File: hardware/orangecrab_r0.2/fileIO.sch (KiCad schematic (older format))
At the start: 29 parts, among them J1 Conn_01x12_Male, J2 Conn_01x16_Male, J3 USB_B_Micro, SW1 SW_Push, U9 CD74HC4067M

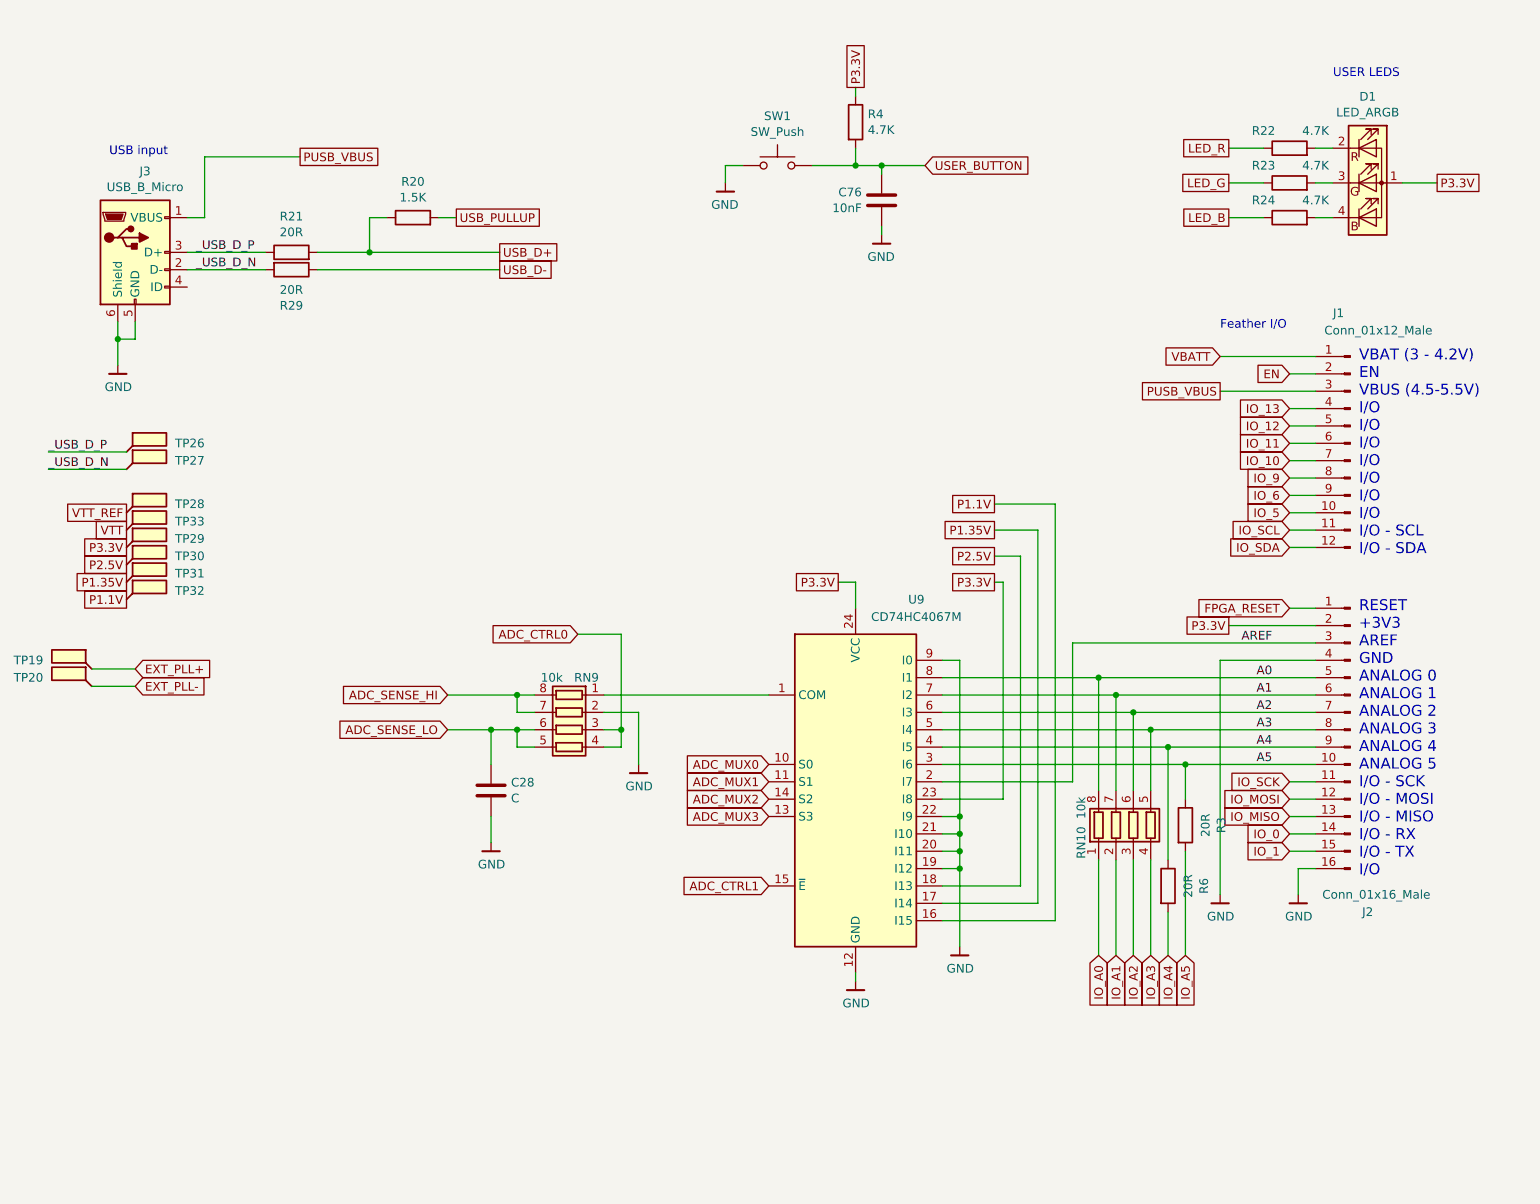
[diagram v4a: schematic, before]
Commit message: hw: Update fiducials Add pullup to FLASH CS/SCK line Update BOM part numbers Fix Button pull-up voltage
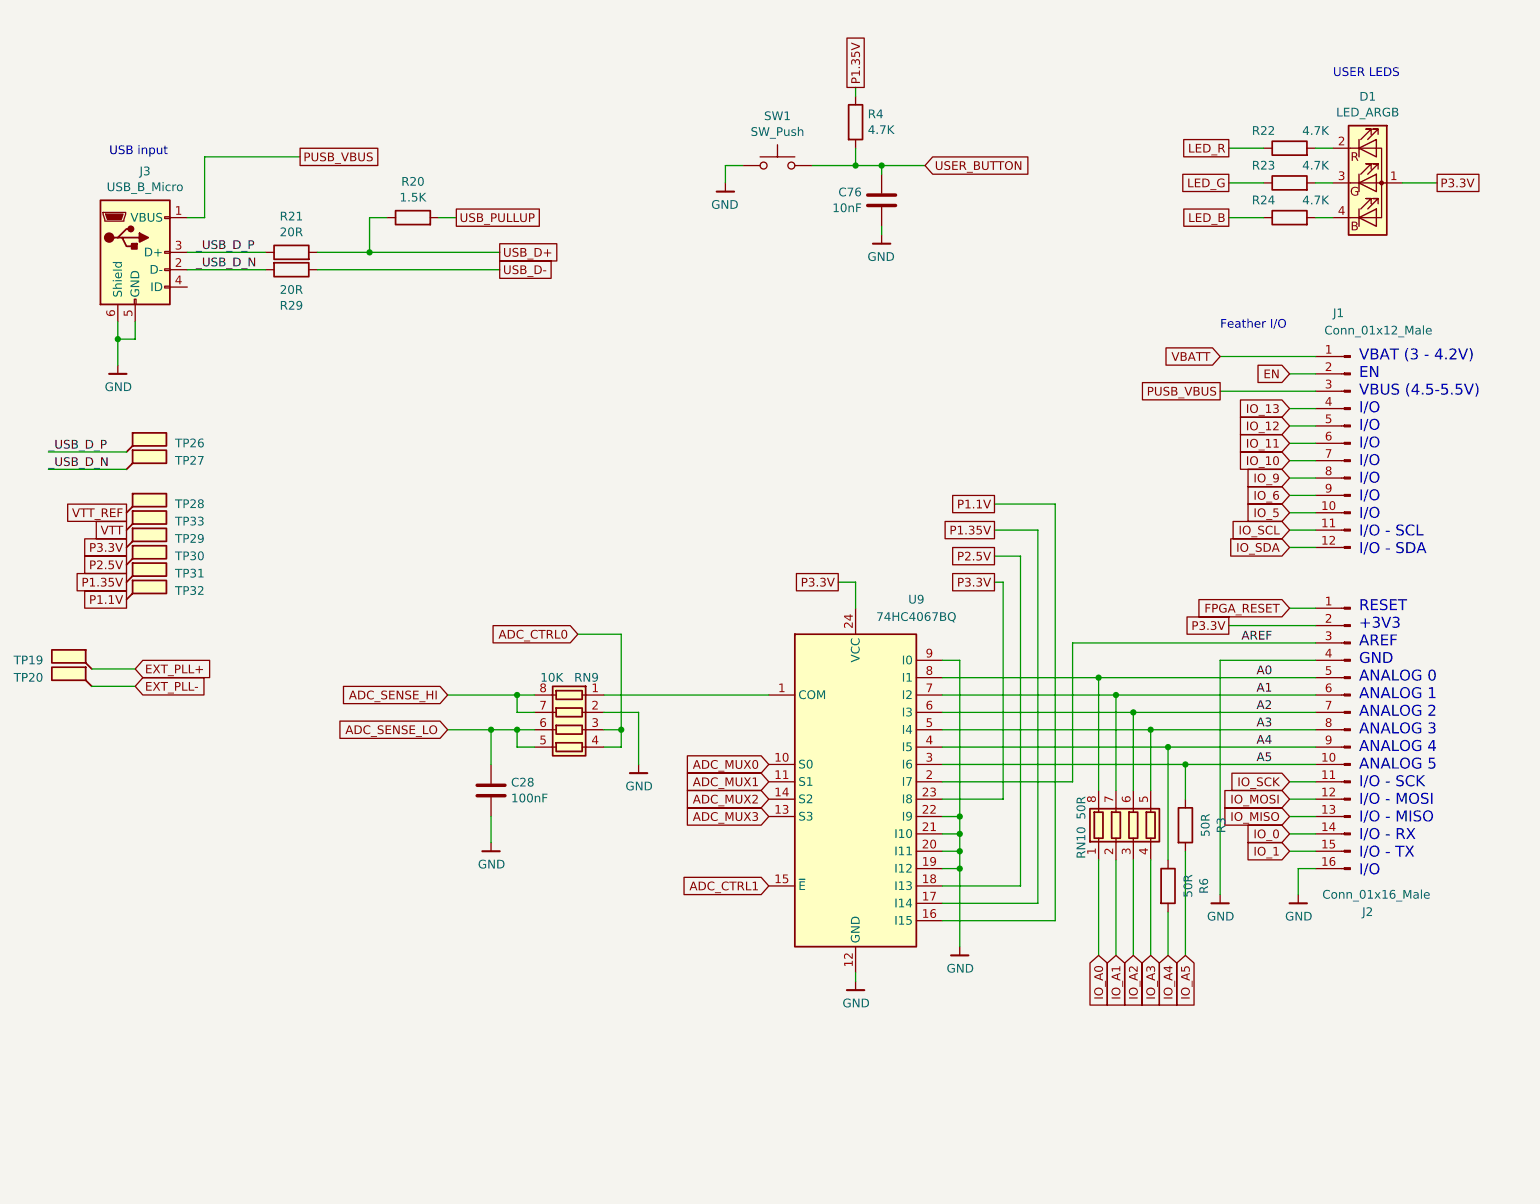
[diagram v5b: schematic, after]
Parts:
- C28: value C -> 100nF; Mfg (none) -> Samsung Electro-Mechanics; PN (none) -> CL03A104KQ3NNNC
- R21, R29: PN (none) -> RC0402FR-0720RL
- R3, R6: value 20R -> 50R; PN (none) -> RC0402FR-0750RL
- RN10: value 10k -> 50R; PN (none) -> RAVF104DJT51R0
- RN9: value 10k -> 10K; PN (none) -> RAVF104DJT10K0
- U9: value CD74HC4067M -> 74HC4067BQ; Mfg (none) -> Nexperia USA Inc.; PN (none) -> 74HC4067BQ,118
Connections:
- net P1.35V: now also R4.1
- net P3.3V: no longer R4.1
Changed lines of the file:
@@
 $EndComp
 Text GLabel 5950 800  1    50   UnSpc ~ 0
-P3.3V
+P1.35V
 $Comp
 L Device:R R4
@@
 F 3 "~" H 2700 1750 50  0001 C CNN
 F 4 "‎Yageo‎" H 2700 1750 50  0001 C CNN "Mfg"
+F 5 "RC0402FR-0720RL" H 2700 1750 50  0001 C CNN "PN"
 	1    2700 1750
 	0    -1   -1   0
@@
 F 3 "~" H 2700 1850 50  0001 C CNN
 F 4 "‎Yageo‎" H 2700 1850 50  0001 C CNN "Mfg"
+F 5 "RC0402FR-0720RL" H 2700 1850 50  0001 C CNN "PN"
 	1    2700 1850
 	0    1    1    0
@@
 P 5950 4800
 F 0 "U9" H 6300 5850 50  0000 C CNN
-F 1 "CD74HC4067M" H 6300 5750 50  0000 C CNN
+F 1 "74HC4067BQ" H 6300 5750 50  0000 C CNN
 F 2 "Package_DFN_QFN:Texas_RGY_R-PVQFN-N24_EP2.05x3.1mm" H 6850 3800 50  0001 C CIN
 F 3 "http://www.ti.com/lit/ds/symlink/cd74hc4067.pdf" H 5600 5650 50  0001 C CNN
+F 4 "Nexperia USA Inc." H 5950 4800 50  0001 C CNN "Mfg"
+F 5 "74HC4067BQ,118" H 5950 4800 50  0001 C CNN "PN"
 	1    5950 4800
 	1    0    0    -1
@@
 AR Path="/5ABC9A87/5DF38AC3" Ref="RN9"  Part="1"
 F 0 "RN9" V 4000 4400 50  0000 C CNN
-F 1 "10k" V 4000 4600 50  0000 C CNN
+F 1 "10K" V 4000 4600 50  0000 C CNN
 F 2 "Resistor_SMD:R_Array_Convex_4x0402" V 4575 4500 50  0001 C CNN
 F 3 "~" H 4300 4500 50  0001 C CNN
 F 4 "Stackpole Electronics Inc" H 4300 4500 50  0001 C CNN "Mfg"
+F 5 "RAVF104DJT10K0" H 4300 4500 50  0001 C CNN "PN"
 	1    4300 4500
 	0    -1   1    0
@@
 P 3850 4850
 F 0 "C28" H 3965 4896 50  0000 L CNN
-F 1 "C" H 3965 4805 50  0000 L CNN
+F 1 "100nF" H 3965 4805 50  0000 L CNN
 F 2 "Capacitor_SMD:C_0201_0603Metric" H 3888 4700 50  0001 C CNN
 F 3 "~" H 3850 4850 50  0001 C CNN
+F 4 "Samsung Electro-Mechanics" H 3850 4850 50  0001 C CNN "Mfg"
+F 5 "CL03A104KQ3NNNC" H 3850 4850 50  0001 C CNN "PN"
 	1    3850 4850
 	1    0    0    -1
@@
 P 7750 5400
 F 0 "R6" V 7957 5400 50  0000 C CNN
-F 1 "20R" V 7866 5400 50  0000 C CNN
+F 1 "50R" V 7866 5400 50  0000 C CNN
 F 2 "Resistor_SMD:R_0201_0603Metric" V 7680 5400 50  0001 C CNN
 F 3 "~" H 7750 5400 50  0001 C CNN
 F 4 "‎Yageo‎" H 7750 5400 50  0001 C CNN "Mfg"
+F 5 "RC0402FR-0750RL" H 7750 5400 50  0001 C CNN "PN"
 	1    7750 5400
 	1    0    0    -1
@@
 P 7850 5050
 F 0 "R3" V 8057 5050 50  0000 C CNN
-F 1 "20R" V 7966 5050 50  0000 C CNN
+F 1 "50R" V 7966 5050 50  0000 C CNN
 F 2 "Resistor_SMD:R_0201_0603Metric" V 7780 5050 50  0001 C CNN
 F 3 "~" H 7850 5050 50  0001 C CNN
 F 4 "‎Yageo‎" H 7850 5050 50  0001 C CNN "Mfg"
+F 5 "RC0402FR-0750RL" H 7850 5050 50  0001 C CNN "PN"
 	1    7850 5050
 	1    0    0    -1
@@
 AR Path="/5ABC9A87/5E8ECDF4" Ref="RN10"  Part="1"
 F 0 "RN10" V 7250 4950 50  0000 C CNN
-F 1 "10k" V 7250 5150 50  0000 C CNN
+F 1 "50R" V 7250 5150 50  0000 C CNN
 F 2 "Resistor_SMD:R_Array_Convex_4x0402" V 7825 5050 50  0001 C CNN
 F 3 "~" H 7550 5050 50  0001 C CNN
 F 4 "Stackpole Electronics Inc" H 7550 5050 50  0001 C CNN "Mfg"
+F 5 "RAVF104DJT51R0" H 7550 5050 50  0001 C CNN "PN"
 	1    7550 5050
 	1    0    0    -1

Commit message: hardware/orangecrab_r0.2: r0.2 Release
Prepared KiCad files for release
Create production folder
Add pdf schematic
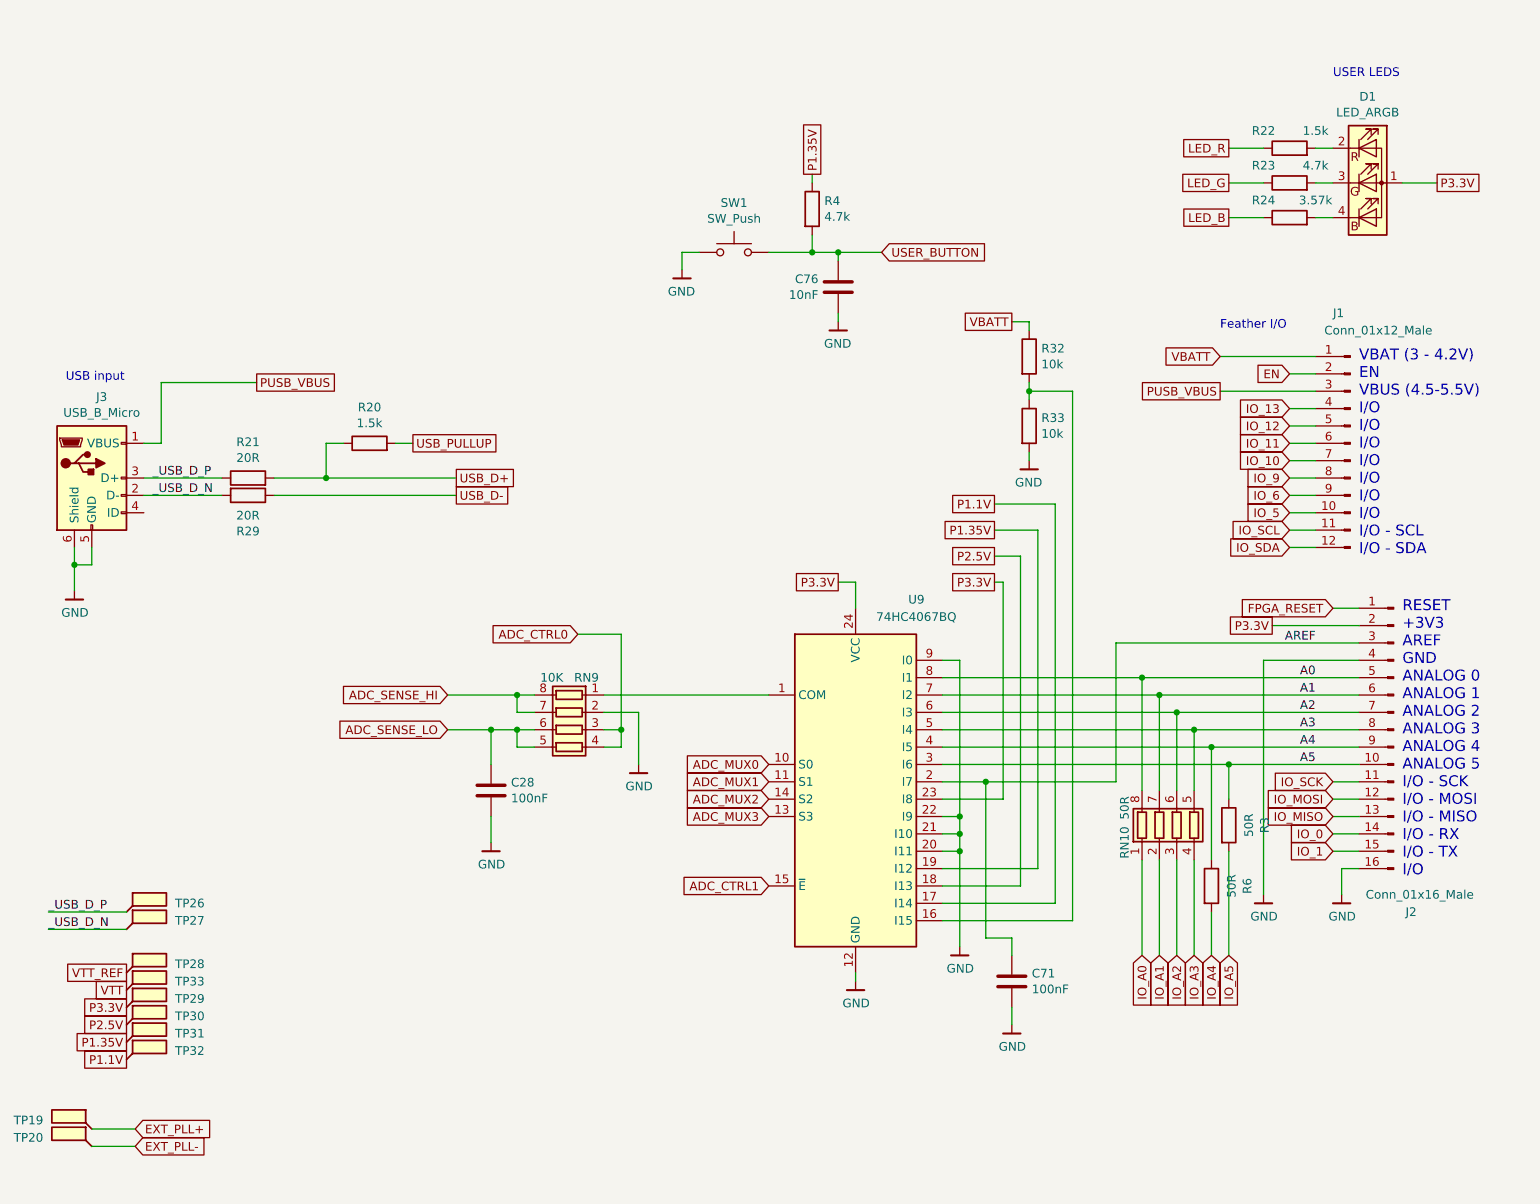
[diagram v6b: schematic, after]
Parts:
- added C71: 100nF, Capacitor_SMD:C_0201_0603Metric, symbol Device:C
- added R32, R33: 10k, Resistor_SMD:R_0201_0603Metric, symbol Device:R
- C76: PN CL03A103KQ3NNNC -> CL03B103KP3NNNC
- R20: value 1.5K -> 1.5k
- R21, R29: PN RC0402FR-0720RL -> RC0201FR-0720RL
- R22: value 4.7K -> 1.5k; PN RC0201FR-074K7L -> RC0201FR-071K5L
- R23, R4: value 4.7K -> 4.7k
- R24: value 4.7K -> 3.57k; PN RC0201FR-074K7L -> RC0201FR-073K57L
- R3, R6: PN RC0402FR-0750RL -> RC0201FR-0750RL
- U9: PN 74HC4067BQ,118 -> 74HC4067BQ\\,118
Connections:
- net AREF: now also C71.1
- net GND: now also C71.2, R33.2; no longer U9.19 (I12)
- net P1.1V: now also U9.17 (I14); no longer U9.16 (I15)
- net P1.35V: now also U9.19 (I12); no longer U9.17 (I14)
- net VBATT: now also R32.1
- new net: R32.2, R33.1, U9.16 (I15)
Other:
- moved on the sheet: C76, J2, J3, R20, R21, R29, R3, R4, R6, RN10, SW1, TP19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
